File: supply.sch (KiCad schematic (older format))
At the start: 89 parts, among them IC1 TPS54561, J10 61300311121, J3 DC_SOCKET, U10 LM3881MME_NOPB, U4 TPS65296, U5 TPS62823DLCT, U9 TPS62823DLCT

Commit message: Update component libraries
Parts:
- C106, C107, C108, C109, C110, C111, C112, C113: footprint antmicro-footprints:0603-cap -> lpddr4-test-board-footprints:0603-cap; symbol antmicroCapacitors0603:C_10n_0603 -> lpddr4-test-board:C_10n_0603
- C116, C117, C118: footprint antmicro-footprints:1206-cap -> lpddr4-test-board-footprints:1206-cap; symbol antmicroCapacitorsmisc:C_47u_16V_1206 -> lpddr4-test-board:C_47u_16V_1206
- S1: footprint antmicro-footprints:Switch_Slide_11.6x4mm_EG1218 -> lpddr4-test-board-footprints:Switch_Slide_11.6x4mm_EG1218; symbol antmicroSlideSwitches:EG1218 -> lpddr4-test-board:EG1218
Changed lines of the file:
@@
 Plane Decoupling
 $Comp
-L antmicroCapacitors0603:C_10n_0603 C106
+L lpddr4-test-board:C_10n_0603 C106
 U 1 1 60003ED3
 P 10550 2925
 F 0 "C106" H 10665 2970 60  0000 L CNN
 F 1 "C_10n_0603" H 10550 2775 60  0001 C CNN
-F 2 "antmicro-footprints:0603-cap" H 10750 3125 60  0001 L CNN
+F 2 "lpddr4-test-board-footprints:0603-cap" H 10750 3125 60  0001 L CNN
 F 3 "" H 10550 2925 50  0001 C CNN
 F 4 "AVX" H 10750 3325 60  0001 L CNN "Manufacturer"
@@
 VDDQ
 $Comp
-L antmicroCapacitors0603:C_10n_0603 C107
+L lpddr4-test-board:C_10n_0603 C107
 U 1 1 6001D22C
 P 11050 2925
 F 0 "C107" H 11165 2970 60  0000 L CNN
 F 1 "C_10n_0603" H 11050 2775 60  0001 C CNN
-F 2 "antmicro-footprints:0603-cap" H 11250 3125 60  0001 L CNN
+F 2 "lpddr4-test-board-footprints:0603-cap" H 11250 3125 60  0001 L CNN
 F 3 "" H 11050 2925 50  0001 C CNN
 F 4 "AVX" H 11250 3325 60  0001 L CNN "Manufacturer"
@@
 VDDQ
 $Comp
-L antmicroCapacitors0603:C_10n_0603 C108
+L lpddr4-test-board:C_10n_0603 C108
 U 1 1 60023729
 P 11475 2950
 F 0 "C108" H 11590 2995 60  0000 L CNN
 F 1 "C_10n_0603" H 11475 2800 60  0001 C CNN
-F 2 "antmicro-footprints:0603-cap" H 11675 3150 60  0001 L CNN
+F 2 "lpddr4-test-board-footprints:0603-cap" H 11675 3150 60  0001 L CNN
 F 3 "" H 11475 2950 50  0001 C CNN
 F 4 "AVX" H 11675 3350 60  0001 L CNN "Manufacturer"
@@
 VDDQ
 $Comp
-L antmicroCapacitors0603:C_10n_0603 C109
+L lpddr4-test-board:C_10n_0603 C109
 U 1 1 60029BE0
 P 11950 2950
 F 0 "C109" H 12065 2995 60  0000 L CNN
 F 1 "C_10n_0603" H 11950 2800 60  0001 C CNN
-F 2 "antmicro-footprints:0603-cap" H 12150 3150 60  0001 L CNN
+F 2 "lpddr4-test-board-footprints:0603-cap" H 12150 3150 60  0001 L CNN
 F 3 "" H 11950 2950 50  0001 C CNN
 F 4 "AVX" H 12150 3350 60  0001 L CNN "Manufacturer"
@@
 1V8_SYS
 $Comp
-L antmicroCapacitors0603:C_10n_0603 C110
+L lpddr4-test-board:C_10n_0603 C110
 U 1 1 60050A58
 P 12575 2975
 F 0 "C110" H 12690 3020 60  0000 L CNN
 F 1 "C_10n_0603" H 12575 2825 60  0001 C CNN
-F 2 "antmicro-footprints:0603-cap" H 12775 3175 60  0001 L CNN
+F 2 "lpddr4-test-board-footprints:0603-cap" H 12775 3175 60  0001 L CNN
 F 3 "" H 12575 2975 50  0001 C CNN
 F 4 "AVX" H 12775 3375 60  0001 L CNN "Manufacturer"
@@
 1V8_SYS
 $Comp
-L antmicroCapacitors0603:C_10n_0603 C111
+L lpddr4-test-board:C_10n_0603 C111
 U 1 1 600519C1
 P 13075 2975
 F 0 "C111" H 13190 3020 60  0000 L CNN
 F 1 "C_10n_0603" H 13075 2825 60  0001 C CNN
-F 2 "antmicro-footprints:0603-cap" H 13275 3175 60  0001 L CNN
+F 2 "lpddr4-test-board-footprints:0603-cap" H 13275 3175 60  0001 L CNN
 F 3 "" H 13075 2975 50  0001 C CNN
 F 4 "AVX" H 13275 3375 60  0001 L CNN "Manufacturer"
@@
 1V8_SYS
 $Comp
-L antmicroCapacitors0603:C_10n_0603 C112
+L lpddr4-test-board:C_10n_0603 C112
 U 1 1 60057FF0
 P 13550 2975
 F 0 "C112" H 13665 3020 60  0000 L CNN
 F 1 "C_10n_0603" H 13550 2825 60  0001 C CNN
-F 2 "antmicro-footprints:0603-cap" H 13750 3175 60  0001 L CNN
+F 2 "lpddr4-test-board-footprints:0603-cap" H 13750 3175 60  0001 L CNN
 F 3 "" H 13550 2975 50  0001 C CNN
 F 4 "AVX" H 13750 3375 60  0001 L CNN "Manufacturer"
@@
 1V8_SYS
 $Comp
-L antmicroCapacitors0603:C_10n_0603 C113
+L lpddr4-test-board:C_10n_0603 C113
 U 1 1 6005E663
 P 14000 2975
 F 0 "C113" H 14115 3020 60  0000 L CNN
 F 1 "C_10n_0603" H 14000 2825 60  0001 C CNN
-F 2 "antmicro-footprints:0603-cap" H 14200 3175 60  0001 L CNN
+F 2 "lpddr4-test-board-footprints:0603-cap" H 14200 3175 60  0001 L CNN
 F 3 "" H 14000 2975 50  0001 C CNN
 F 4 "AVX" H 14200 3375 60  0001 L CNN "Manufacturer"
@@
 $EndComp
 $Comp
-L antmicroSlideSwitches:EG1218 S1
+L lpddr4-test-board:EG1218 S1
 U 1 1 602873C2
 P 10350 8725
 F 0 "S1" H 10350 9006 50  0000 C CNN
 F 1 "EG1218" H 10350 8915 50  0000 C CNN
-F 2 "antmicro-footprints:Switch_Slide_11.6x4mm_EG1218" H 10550 8925 50  0001 L CNN
+F 2 "lpddr4-test-board-footprints:Switch_Slide_11.6x4mm_EG1218" H 10550 8925 50  0001 L CNN
 F 3 "http://spec_sheets.e-switch.com/specs/P040040.pdf" H 10550 9025 60  0001 L CNN
 F 4 "EG1218" H 10550 9225 60  0001 L CNN "MPN"
@@
 	10675 8825 10675 9000
 $Comp
-L antmicroCapacitorsmisc:C_47u_16V_1206 C116
+L lpddr4-test-board:C_47u_16V_1206 C116
 U 1 1 602EDD65
 P 1000 5300
 F 0 "C116" H 1115 5345 60  0000 L CNN
 F 1 "C_47u_16V_1206" H 1000 5150 60  0001 C CNN
-F 2 "antmicro-footprints:1206-cap" H 1200 5500 60  0001 L CNN
+F 2 "lpddr4-test-board-footprints:1206-cap" H 1200 5500 60  0001 L CNN
 F 3 "" H 1000 5300 50  0001 C CNN
 F 4 "TDK" H 1200 5700 60  0001 L CNN "Manufacturer"
@@
 $EndComp
 $Comp
-L antmicroCapacitorsmisc:C_47u_16V_1206 C117
+L lpddr4-test-board:C_47u_16V_1206 C117
 U 1 1 602EFA5A
 P 1575 5300
 F 0 "C117" H 1690 5345 60  0000 L CNN
 F 1 "C_47u_16V_1206" H 1575 5150 60  0001 C CNN
-F 2 "antmicro-footprints:1206-cap" H 1775 5500 60  0001 L CNN
+F 2 "lpddr4-test-board-footprints:1206-cap" H 1775 5500 60  0001 L CNN
 F 3 "" H 1575 5300 50  0001 C CNN
 F 4 "TDK" H 1775 5700 60  0001 L CNN "Manufacturer"
@@
 $EndComp
 $Comp
-L antmicroCapacitorsmisc:C_47u_16V_1206 C118
+L lpddr4-test-board:C_47u_16V_1206 C118
 U 1 1 602EFC89
 P 2150 5300
 F 0 "C118" H 2265 5345 60  0000 L CNN
 F 1 "C_47u_16V_1206" H 2150 5150 60  0001 C CNN
-F 2 "antmicro-footprints:1206-cap" H 2350 5500 60  0001 L CNN
+F 2 "lpddr4-test-board-footprints:1206-cap" H 2350 5500 60  0001 L CNN
 F 3 "" H 2150 5300 50  0001 C CNN
 F 4 "TDK" H 2350 5700 60  0001 L CNN "Manufacturer"

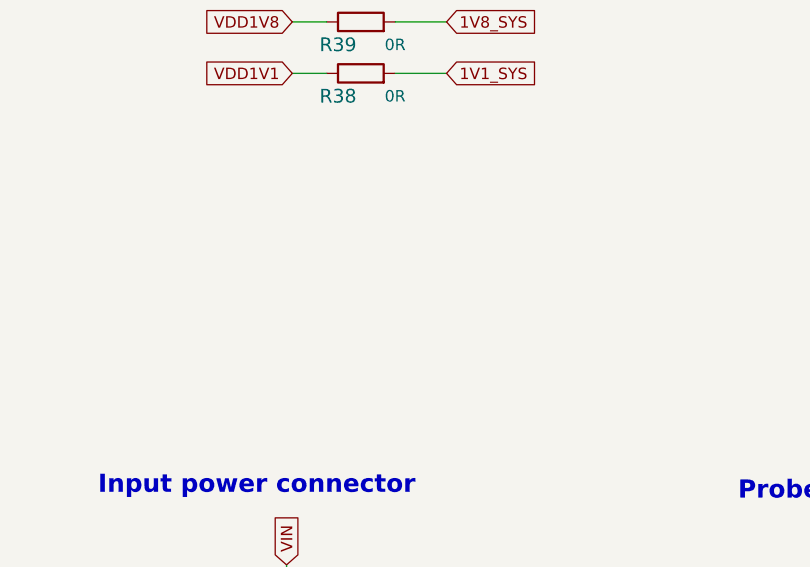
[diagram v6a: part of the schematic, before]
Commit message: Start rev. 1.0.1 Add FAN connector
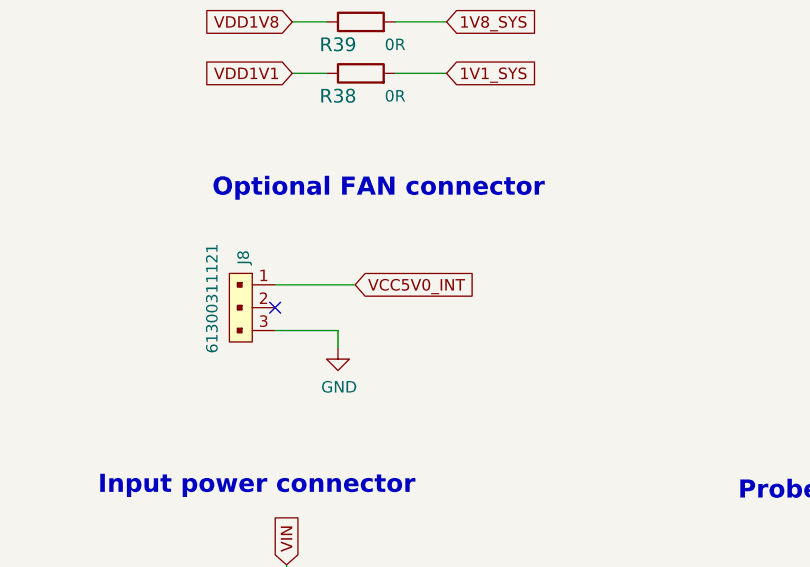
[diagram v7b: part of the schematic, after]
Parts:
- added J8: 61300311121, lpddr4-test-board-footprints:PinHeader_1x3_P2.54_Drill1.1mm, symbol lpddr4-test-board:61300311121
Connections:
- net GND: now also J8.3
- net VCC5V0_INT: now also J8.1
- no-connect marks 2 -> 3
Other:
- note added: "Optional FAN connector"
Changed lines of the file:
@@
 Title "LPDDR4 Test Board"
 Date ""
-Rev "1.0.0"
+Rev "1.0.1"
 Comp ""
 Comment1 ""
@@
 Wire Wire Line
 	12725 8425 12725 8525
+Text Notes 12400 6825 0    79   ~ 16
+Optional FAN connector
+$Comp
+L lpddr4-test-board:61300311121 J8
+U 1 1 60001A7D
+P 12525 7200
+F 0 "J8" H 12437 7212 50  0000 R CNN
+F 1 "61300311121" H 12825 7075 50  0000 R CNN
+F 2 "lpddr4-test-board-footprints:PinHeader_1x3_P2.54_Drill1.1mm" H 12725 7400 60  0001 L CNN
+F 3 "https://katalog.we-online.de/em/datasheet/6130xx11121.pdf" H 12725 7500 60  0001 L CNN
+F 4 "61300311121" H 12725 7700 60  0001 L CNN "MPN"
+F 5 "Wurth Electronics Inc." H 12725 8300 60  0001 L CNN "Manufacturer"
+	1    12525 7200
+	0    1    1    0
+$EndComp
+$Comp
+L lpddr4-test-board:GND #PWR036
+U 1 1 60003077
+P 12950 7475
+F 0 "#PWR036" H 12950 7225 50  0001 C CNN
+F 1 "GND" H 12955 7302 50  0000 C CNN
+F 2 "" H 12950 7475 50  0001 C CNN
+F 3 "" H 12950 7475 50  0001 C CNN
+	1    12950 7475
+	1    0    0    -1
+$EndComp
+Wire Wire Line
+	12675 7400 12950 7400
+Wire Wire Line
+	12950 7400 12950 7475
+Text GLabel 13025 7200 2    50   Input ~ 0
+VCC5V0_INT
+Wire Wire Line
+	12675 7200 13025 7200
+NoConn ~ 12675 7300
 $EndSCHEMATC

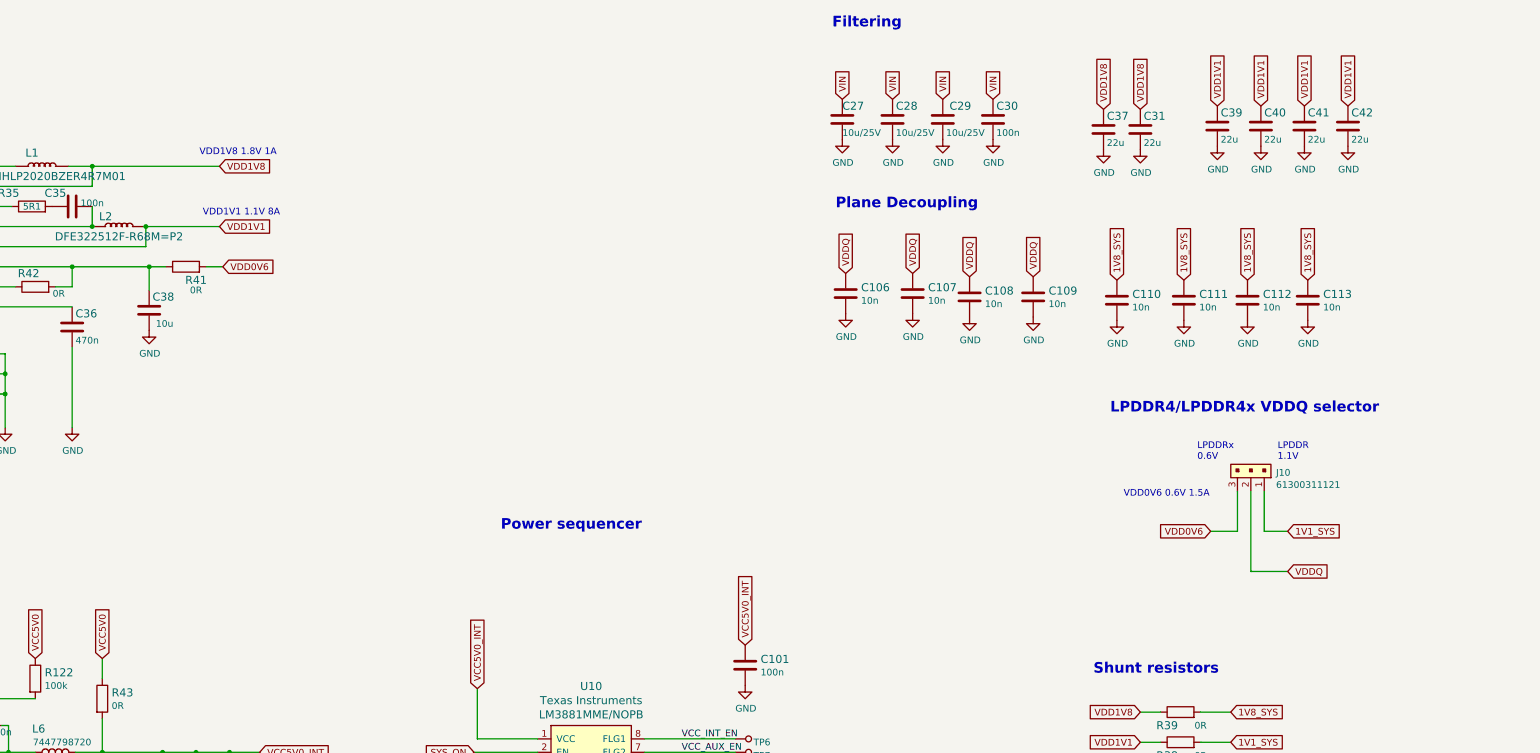
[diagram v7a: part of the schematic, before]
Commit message: Change ETH PHY to KSZ9031RNXCA supporting 1GbE
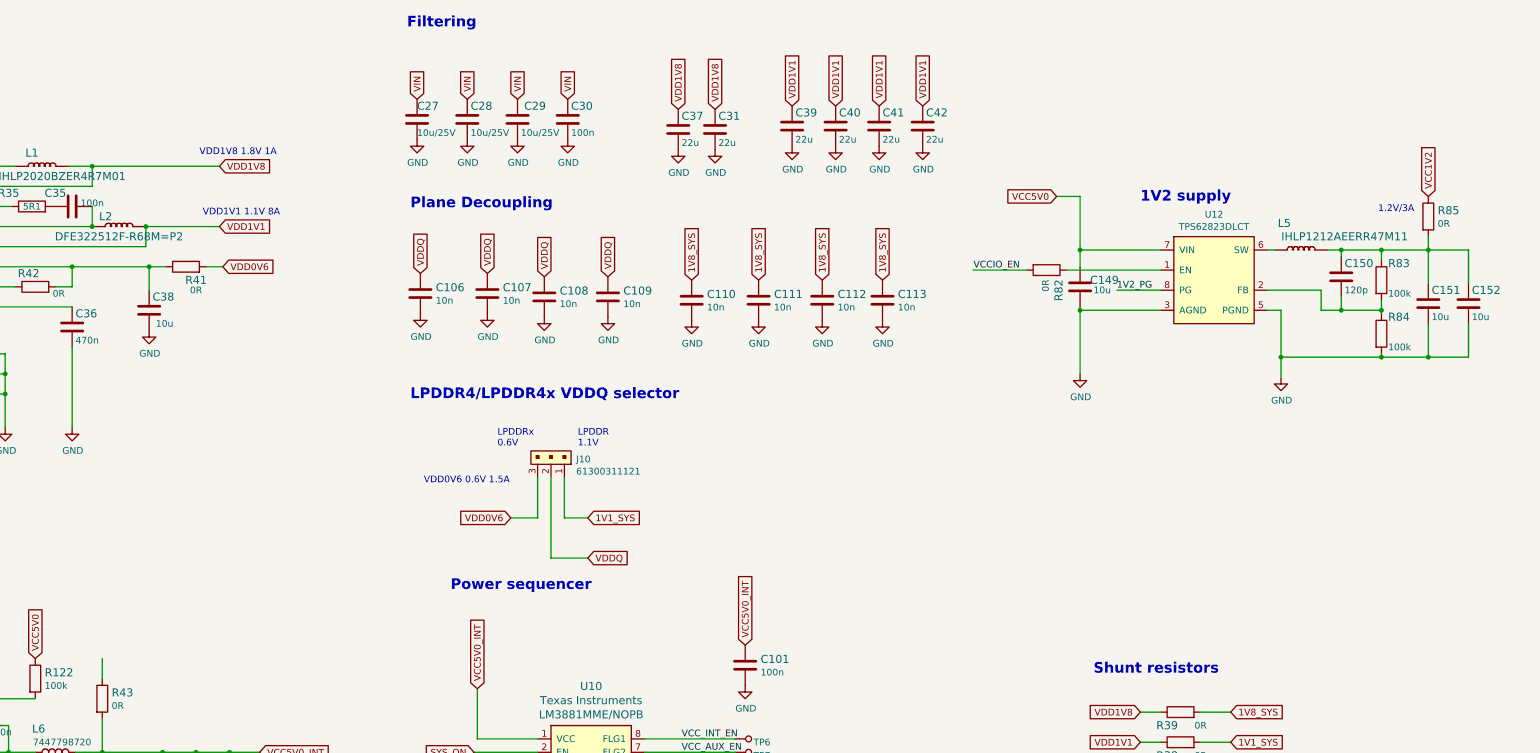
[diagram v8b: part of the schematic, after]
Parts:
- added C149, C151: C_10u_0402, artix-dc-scm-footprints:0402-cap, symbol lpddr4-test-board:C_10u_0402
- added C150: C_120p_0402, artix-dc-scm-footprints:0402-res, symbol antmicroCapacitors0402:C_120p_0402
- added C152: C_10u_0402, artix-dc-scm-footprints:0402-cap, symbol antmicroCapacitors0402:C_10u_0402
- added L5: IHLP1212AEERR47M11, artix-dc-scm-footprints:IHLP-1212AE, symbol lpddr4-test-board:IHLP1212AEERR47M11
- added R82: R_0R_0402, artix-dc-scm-footprints:0402-res, symbol lpddr4-test-board:R_0R_0402
- added R83, R84: R_100k_0402, artix-dc-scm-footprints:0402-res, symbol lpddr4-test-board:R_100k_0402
- added R85: R_0R_0603, artix-dc-scm-footprints:0603-res, symbol lpddr4-test-board:R_0R_0603
- added U12: TPS62823DLCT, artix-dc-scm-footprints:QFN-8_2x1mm, symbol lpddr4-test-board:TPS62823DLCT
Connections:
- net GND: now also C149.2, C151.2, C152.2, R84.2, U12.3 (AGND), U12.5 (PGND)
- net VCC5V0: now also C149.1, U12.7 (VIN); no longer R43.1
- new net: R82.1, U12.1 (EN)
- new net: C150.2, R83.2, R84.1, U12.2 (FB)
- new net: L5.1 (P), U12.6 (SW)
- new net: C150.1, C151.1, C152.1, L5.2 (P), R83.1, R85.2
- new net 1V2_PG: U12.8 (PG)
- new net VCC1V2: R85.1
- new net VCCIO_EN: R82.2
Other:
- note added: "1.2V/3A"
- note added: "1V2 supply"
- moved on the sheet: C106, C107, C108, C109, C110, C111, C112, C113, C27, C28, C29, C30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
